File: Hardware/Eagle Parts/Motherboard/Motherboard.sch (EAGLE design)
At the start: 33 parts, among them J2 U.FL, U1 MK10DN512ZVLL10, U10 MPL115A, U5 ATMEGA8U2AU, U9 MPL3115A2LGA8

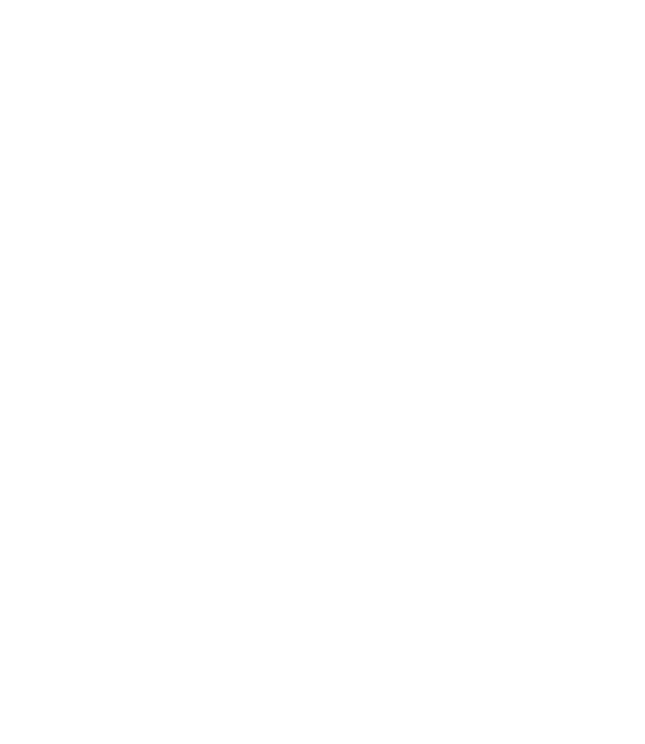
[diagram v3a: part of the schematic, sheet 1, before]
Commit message: Added JTAG Connector and Moved Some Stuff Around
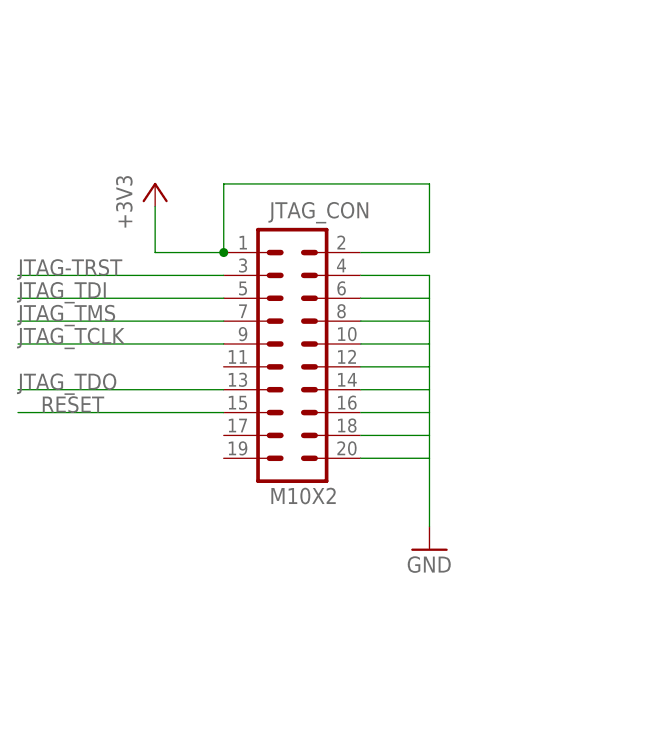
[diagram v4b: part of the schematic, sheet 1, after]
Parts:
- added JTAG_CON: M10X2, SparkFun-Connectors:M10X2
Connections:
- new net +3V3: JTAG_CON.1, JTAG_CON.2
- new net JTAG-TRST: JTAG_CON.3
- new net JTAG_TCLK: JTAG_CON.9
- new net JTAG_TDI: JTAG_CON.5
- new net JTAG_TDO: JTAG_CON.13
- new net JTAG_TMS: JTAG_CON.7
- new net RESET: JTAG_CON.15
- net GND: now also JTAG_CON.10, JTAG_CON.12, JTAG_CON.14, JTAG_CON.16, JTAG_CON.18, JTAG_CON.20, JTAG_CON.4, JTAG_CON.6, JTAG_CON.8
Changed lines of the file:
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@@
 <part name="C2" library="SparkFun-Passives" deviceset="CAP" device="PTH1"/>
 <part name="GND9" library="supply1" deviceset="GND" device=""/>
+<part name="JTAG_CON" library="SparkFun-Connectors" deviceset="M10X2" device=""/>
+<part name="+3V5" library="supply1" deviceset="+3V3" device=""/>
+<part name="GND10" library="supply1" deviceset="GND" device=""/>
 </parts>
 <sheets>
@@
 <instance part="C2" gate="G$1" x="-210.82" y="111.76" rot="R270"/>
 <instance part="GND9" gate="1" x="-218.44" y="109.22" rot="R270"/>
+<instance part="JTAG_CON" gate="G$1" x="-281.94" y="134.62"/>
+<instance part="+3V5" gate="G$1" x="-297.18" y="152.4"/>
+<instance part="GND10" gate="1" x="-266.7" y="111.76"/>
 </instances>
 <busses>
@@
 <wire x1="-215.9" y1="106.68" x2="-213.36" y2="106.68" width="0.1524" layer="91"/>
 </segment>
+<segment>
+<pinref part="JTAG_CON" gate="G$1" pin="4"/>
+<wire x1="-274.32" y1="142.24" x2="-266.7" y2="142.24" width="0.1524" layer="91"/>
+<pinref part="JTAG_CON" gate="G$1" pin="6"/>
+<wire x1="-274.32" y1="139.7" x2="-266.7" y2="139.7" width="0.1524" layer="91"/>
+<wire x1="-266.7" y1="142.24" x2="-266.7" y2="139.7" width="0.1524" layer="91"/>
+<pinref part="JTAG_CON" gate="G$1" pin="8"/>
+<wire x1="-274.32" y1="137.16" x2="-266.7" y2="137.16" width="0.1524" layer="91"/>
+<wire x1="-266.7" y1="139.7" x2="-266.7" y2="137.16" width="0.1524" layer="91"/>
+<pinref part="JTAG_CON" gate="G$1" pin="10"/>
+<wire x1="-274.32" y1="134.62" x2="-266.7" y2="134.62" width="0.1524" layer="91"/>
+<wire x1="-266.7" y1="137.16" x2="-266.7" y2="134.62" width="0.1524" layer="91"/>
+<pinref part="JTAG_CON" gate="G$1" pin="12"/>
+<wire x1="-274.32" y1="132.08" x2="-266.7" y2="132.08" width="0.1524" layer="91"/>
+<wire x1="-266.7" y1="134.62" x2="-266.7" y2="132.08" width="0.1524" layer="91"/>
+<pinref part="JTAG_CON" gate="G$1" pin="14"/>
+<wire x1="-274.32" y1="129.54" x2="-266.7" y2="129.54" width="0.1524" layer="91"/>
+<wire x1="-266.7" y1="132.08" x2="-266.7" y2="129.54" width="0.1524" layer="91"/>
+<pinref part="JTAG_CON" gate="G$1" pin="20"/>
+<wire x1="-274.32" y1="121.92" x2="-266.7" y2="121.92" width="0.1524" layer="91"/>
+<pinref part="JTAG_CON" gate="G$1" pin="16"/>
+<wire x1="-274.32" y1="127" x2="-266.7" y2="127" width="0.1524" layer="91"/>
+<wire x1="-266.7" y1="127" x2="-266.7" y2="124.46" width="0.1524" layer="91"/>
+<wire x1="-266.7" y1="124.46" x2="-266.7" y2="121.92" width="0.1524" layer="91"/>
+<pinref part="JTAG_CON" gate="G$1" pin="18"/>
+<wire x1="-274.32" y1="124.46" x2="-266.7" y2="124.46" width="0.1524" layer="91"/>
+<wire x1="-266.7" y1="129.54" x2="-266.7" y2="127" width="0.1524" layer="91"/>
+<wire x1="-266.7" y1="121.92" x2="-266.7" y2="114.3" width="0.1524" layer="91"/>
+<pinref part="GND10" gate="1" pin="GND"/>
+</segment>
 </net>
 <net name="CLKO" class="0">
@@
 </segment>
 </net>
+<net name="RESET" class="0">
+<segment>
+<pinref part="JTAG_CON" gate="G$1" pin="15"/>
+<wire x1="-289.56" y1="127" x2="-312.42" y2="127" width="0.1524" layer="91"/>
+<label x="-309.88" y="127" size="1.778" layer="95"/>
+</segment>
+</net>
+<net name="JTAG_TCLK" class="0">
+<segment>
+<pinref part="JTAG_CON" gate="G$1" pin="9"/>
+<wire x1="-289.56" y1="134.62" x2="-312.42" y2="134.62" width="0.1524" layer="91"/>
+<label x="-312.42" y="134.62" size="1.778" layer="95"/>
+</segment>
+</net>
+<net name="JTAG_TDI" class="0">
+<segment>
+<pinref part="JTAG_CON" gate="G$1" pin="5"/>
+<wire x1="-289.56" y1="139.7" x2="-312.42" y2="139.7" width="0.1524" layer="91"/>
+<label x="-312.42" y="139.7" size="1.778" layer="95"/>
+</segment>
+</net>
+<net name="JTAG_TDO" class="0">
+<segment>
+<pinref part="JTAG_CON" gate="G$1" pin="13"/>
+<wire x1="-289.56" y1="129.54" x2="-312.42" y2="129.54" width="0.1524" layer="91"/>
+<label x="-312.42" y="129.54" size="1.778" layer="95"/>
+</segment>
+</net>
+<net name="JTAG_TMS" class="0">
+<segment>
+<pinref part="JTAG_CON" gate="G$1" pin="7"/>
+<wire x1="-289.56" y1="137.16" x2="-312.42" y2="137.16" width="0.1524" layer="91"/>
+<label x="-312.42" y="137.16" size="1.778" layer="95"/>
+</segment>
+</net>
+<net name="JTAG-TRST" class="0">
+<segment>
+<pinref part="JTAG_CON" gate="G$1" pin="3"/>
+<wire x1="-289.56" y1="142.24" x2="-312.42" y2="142.24" width="0.1524" layer="91"/>
+<label x="-312.42" y="142.24" size="1.778" layer="95"/>
+</segment>
+</net>
+<net name="+3V3" class="0">
+<segment>
+<pinref part="JTAG_CON" gate="G$1" pin="1"/>
+<pinref part="JTAG_CON" gate="G$1" pin="2"/>
+<wire x1="-274.32" y1="144.78" x2="-266.7" y2="144.78" width="0.1524" layer="91"/>
+<wire x1="-266.7" y1="144.78" x2="-266.7" y2="152.4" width="0.1524" layer="91"/>
+<wire x1="-266.7" y1="152.4" x2="-289.56" y2="152.4" width="0.1524" layer="91"/>
+<wire x1="-289.56" y1="152.4" x2="-289.56" y2="144.78" width="0.1524" layer="91"/>
+<pinref part="+3V5" gate="G$1" pin="+3V3"/>
+<wire x1="-289.56" y1="144.78" x2="-297.18" y2="144.78" width="0.1524" layer="91"/>
+<wire x1="-297.18" y1="144.78" x2="-297.18" y2="149.86" width="0.1524" layer="91"/>
+<junction x="-289.56" y="144.78"/>
+</segment>
+</net>

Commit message: Connected JTAG Connector
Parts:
- removed U$1: W5500, w5500_wiznet:W5500
- removed U$2: SPBT2632C2A, SPBT2632C2A:SPBT2632C2A
- removed U5: ATMEGA8U2AU, SparkFun-DigitalIC:ATMEGA8U2AU
- added U$12: W5500, w5500_wiznet:W5500
- added U$13: SPBT2632C2A, SPBT2632C2A:SPBT2632C2A
- added U2: ATMEGA8U2AU, SparkFun-DigitalIC:ATMEGA8U2AU
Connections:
- removed net RESET: JTAG_CON.15
- new net JTAG_TRST_B: JTAG_CON.15, U1A.PTA5
- net GND: now also U1A.VSS, U1A.VSSA, U1A.VSS_2, U1A.VSS_3
- net JTAG_TCLK: now also U1A.PTA0
- net JTAG_TDI: now also U1A.PTA1
- net JTAG_TDO: now also U1A.PTA2
- net JTAG_TMS: now also U1A.PTA3
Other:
- note removed: "Main Processor"

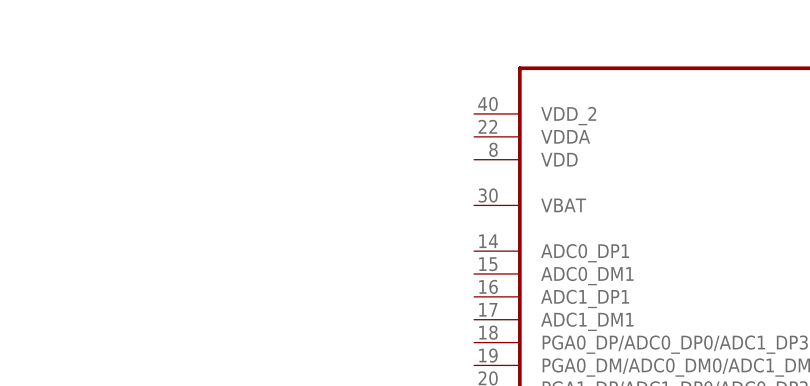
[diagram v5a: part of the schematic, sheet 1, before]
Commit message: Wired power to part of main processor
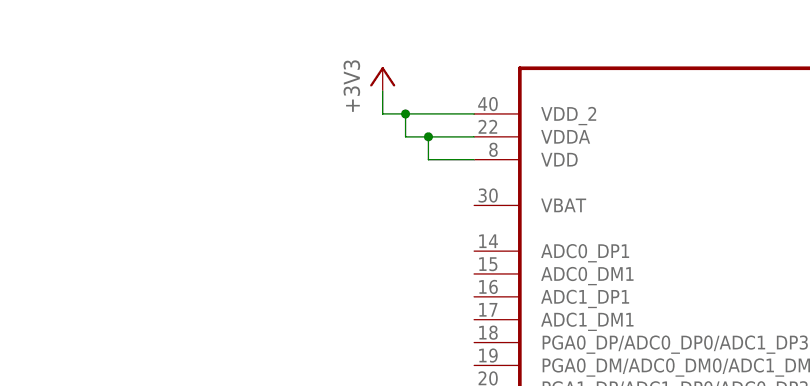
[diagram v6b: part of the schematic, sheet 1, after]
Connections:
- net +3V3: now also U1A.VDD, U1A.VDDA, U1A.VDD_2
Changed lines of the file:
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@@
 <part name="U$12" library="w5500_wiznet" deviceset="W5500" device=""/>
 <part name="U$13" library="SPBT2632C2A" deviceset="SPBT2632C2A" device=""/>
+<part name="+3V1" library="supply1" deviceset="+3V3" device=""/>
 </parts>
 <sheets>
@@
 <instance part="GND10" gate="1" x="-132.08" y="60.96"/>
 <instance part="GND11" gate="1" x="-63.5" y="22.86" rot="R270"/>
+<instance part="+3V1" gate="G$1" x="-58.42" y="129.54"/>
 </instances>
 <busses>
@@
 <junction x="-154.94" y="93.98"/>
 </segment>
-</net>
+<segment>
+<pinref part="U1" gate="A" pin="VDD_2"/>
+<pinref part="+3V1" gate="G$1" pin="+3V3"/>
+<wire x1="-48.26" y1="124.46" x2="-55.88" y2="124.46" width="0.1524" layer="91"/>
+<wire x1="-55.88" y1="124.46" x2="-58.42" y2="124.46" width="0.1524" layer="91"/>
+<wire x1="-58.42" y1="124.46" x2="-58.42" y2="127" width="0.1524" layer="91"/>
+<pinref part="U1" gate="A" pin="VDDA"/>
+<wire x1="-48.26" y1="121.92" x2="-53.34" y2="121.92" width="0.1524" layer="91"/>
+<wire x1="-53.34" y1="121.92" x2="-55.88" y2="121.92" width="0.1524" layer="91"/>
+<wire x1="-55.88" y1="121.92" x2="-55.88" y2="124.46" width="0.1524" layer="91"/>
+<junction x="-55.88" y="124.46"/>
+<pinref part="U1" gate="A" pin="VDD"/>
+<wire x1="-48.26" y1="119.38" x2="-53.34" y2="119.38" width="0.1524" layer="91"/>
+<wire x1="-53.34" y1="119.38" x2="-53.34" y2="121.92" width="0.1524" layer="91"/>
+<junction x="-53.34" y="121.92"/>
+</segment>
+</net>

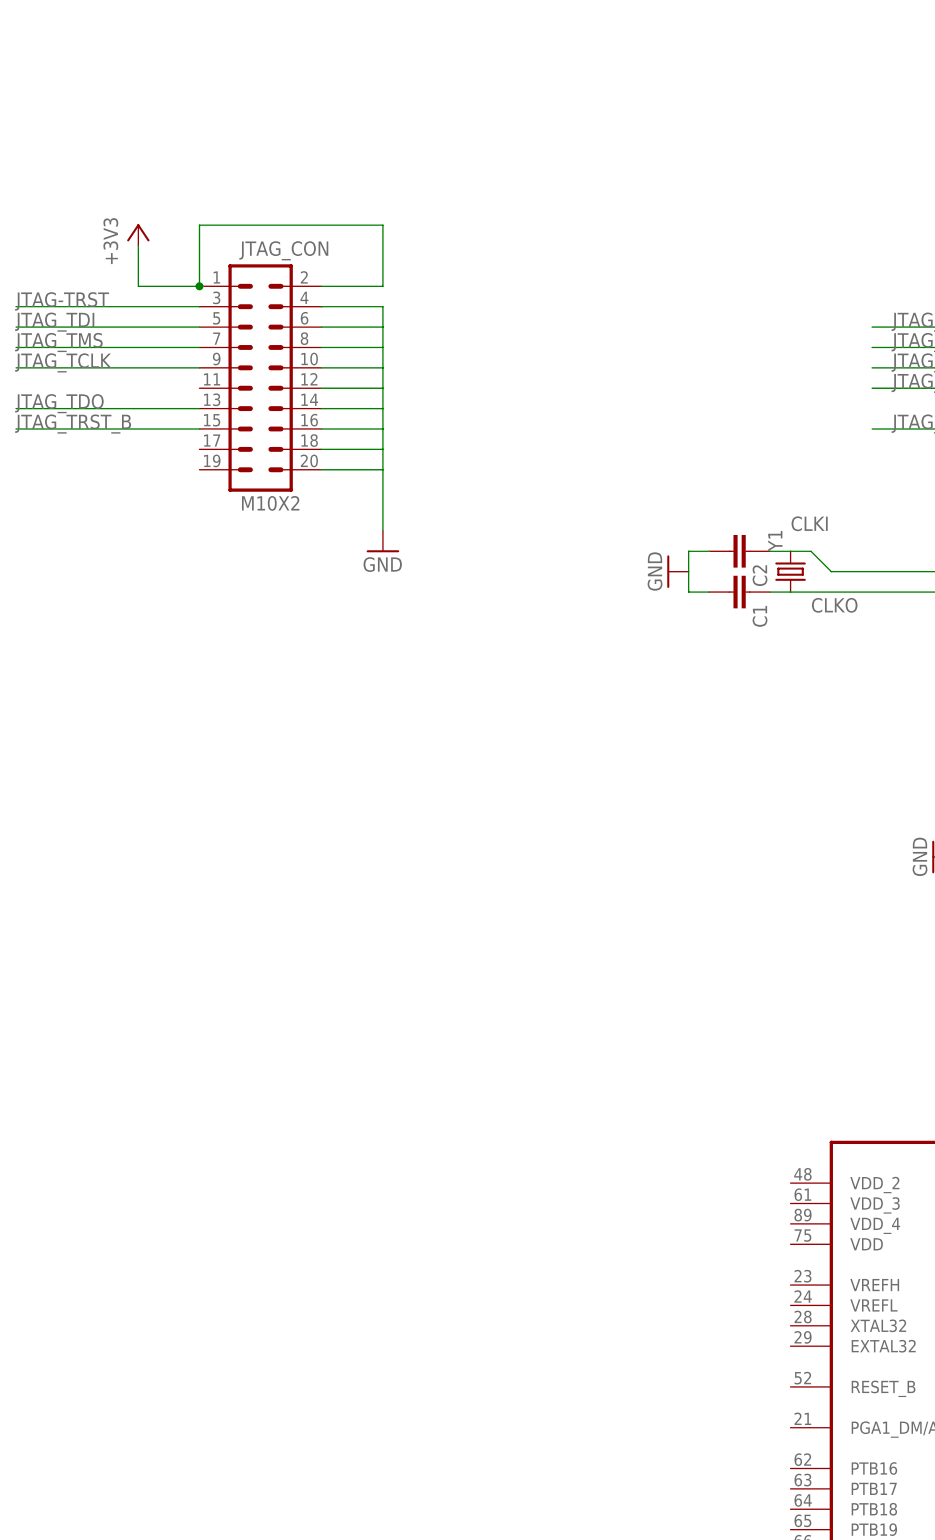
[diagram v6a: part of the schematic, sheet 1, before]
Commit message: Added Reset Switch to Main Processor
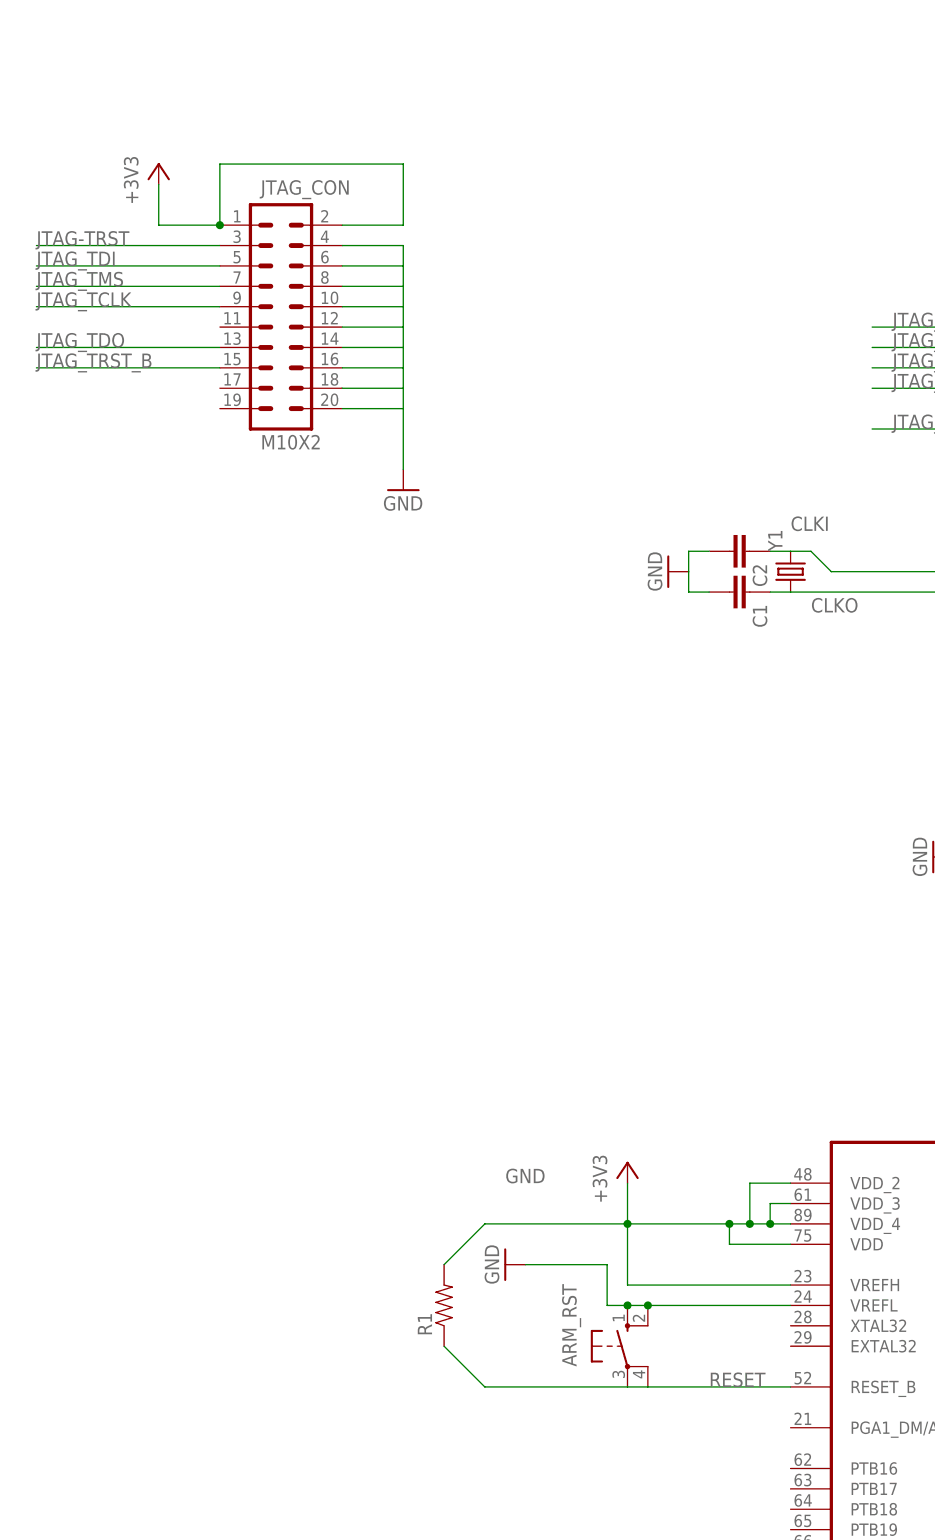
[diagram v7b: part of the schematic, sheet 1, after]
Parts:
- added ARM_RST: (no value), switch-omron:10-XX
- added R1: (no value), SparkFun-Resistors:RESISTORPTH-1/4W
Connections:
- new net RESET: ARM_RST.P, ARM_RST.P1, R1.1, U1B.RESET_B
- net +3V3: now also R1.2, U1B.VDD, U1B.VDD_2, U1B.VDD_3, U1B.VDD_4, U1B.VREFH
- net GND: now also ARM_RST.S, ARM_RST.S1, U1B.VREFL
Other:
- moved on the sheet: JTAG_CON

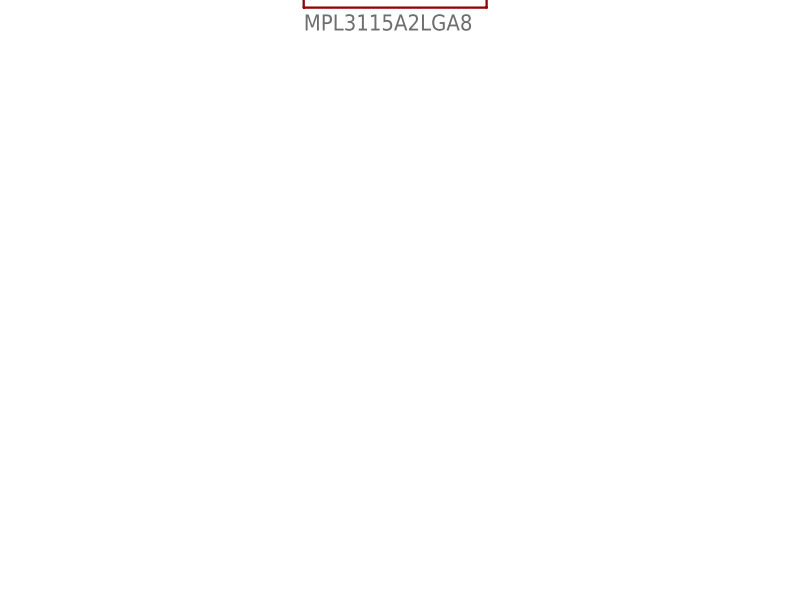
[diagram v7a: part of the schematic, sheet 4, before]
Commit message: Added Mux to Schematic
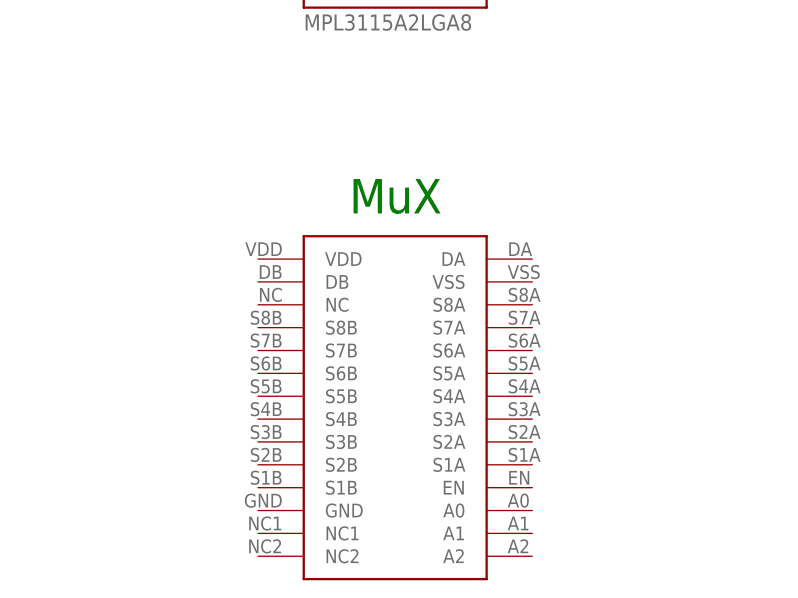
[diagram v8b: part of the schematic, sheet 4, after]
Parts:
- added U$1: ADG1407, adg1407:ADG1407
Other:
- note added: "MuX"
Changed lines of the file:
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@@
 <part name="GND12" library="supply1" deviceset="GND" device=""/>
 <part name="+3V3" library="supply1" deviceset="+3V3" device=""/>
+<part name="U$1" library="adg1407" deviceset="ADG1407" device=""/>
 </parts>
 <sheets>
@@
 <text x="248.92" y="68.58" size="5.08" layer="91">TCP/Eth</text>
 <text x="251.46" y="-30.48" size="5.08" layer="91">Bluetooth</text>
+<text x="-25.4" y="-63.5" size="3.81" layer="91">MuX</text>
 </plain>
 <instances>
@@
 <instance part="U$12" gate="G$1" x="246.38" y="0"/>
 <instance part="U$13" gate="G$1" x="269.24" y="-55.88"/>
+<instance part="U$1" gate="G$1" x="-20.32" y="-86.36"/>
 </instances>
 <busses>
